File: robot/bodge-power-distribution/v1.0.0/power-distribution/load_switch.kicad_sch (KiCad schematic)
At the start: 15 parts, among them Q1 SQJA80EP-T1_GE3, Q2 SQJA80EP-T1_GE3, U1 LTC4367

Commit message: Update load switch
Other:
- note added: "Alt FETs: SQJA90EP-T1_GE3 SQJA92EP-T1_GE3"
- note added: "The voltage divider draws ~3uA, which is less than the 5uA-20uA of the LTC4367"
- note removed: "Alt: SQJA90EP-T1_GE3, SQJA92EP-T1_GE3"
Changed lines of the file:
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@@
+    (effects (font (size 1.27 1.27)) (justify left bottom))
+  )
+  (text "The voltage divider draws ~3uA,\nwhich is less than the 5uA-20uA of the LTC4367 "
+    (at 85.09 97.79 0)
     (effects (font (size 1.27 1.27)) (justify left bottom))
   )
@@
     (effects (font (size 1.27 1.27)) (justify left bottom))
   )
-  (text "Alt: SQJA90EP-T1_GE3, SQJA92EP-T1_GE3 " (at 149.86 38.1 0)
+  (text "Alt FETs:\n  SQJA90EP-T1_GE3\n  SQJA92EP-T1_GE3 " (at 147.32 36.83 0)
     (effects (font (size 1.27 1.27)) (justify left bottom))
   )

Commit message: Reorganize
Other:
- title: Power Distribution -> Bodge Control
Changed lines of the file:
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@@
   (paper "A4")
   (title_block
-    (title "Power Distribution")
-    (date "2021-11-14")
+    (title "Bodge Control")
+    (date "2022-11-06")
     (rev "1.0.0")
     (company "The A-Team (RC SSL)")

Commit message: Sync
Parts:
- added R?: 100k, Resistor_SMD:R_0402_1005Metric_Pad0.72x0.64mm_HandSolder, symbol Device:R_Small_US
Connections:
- net V_{BATT(PROTECTED)}: now also R?.1
- net ~{FAULT} renamed PGOOD_{LoadSwitch}
- net PGOOD_{LoadSwitch}: now also R?.2
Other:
- moved on the sheet: C1, C2, C3, C4, R10

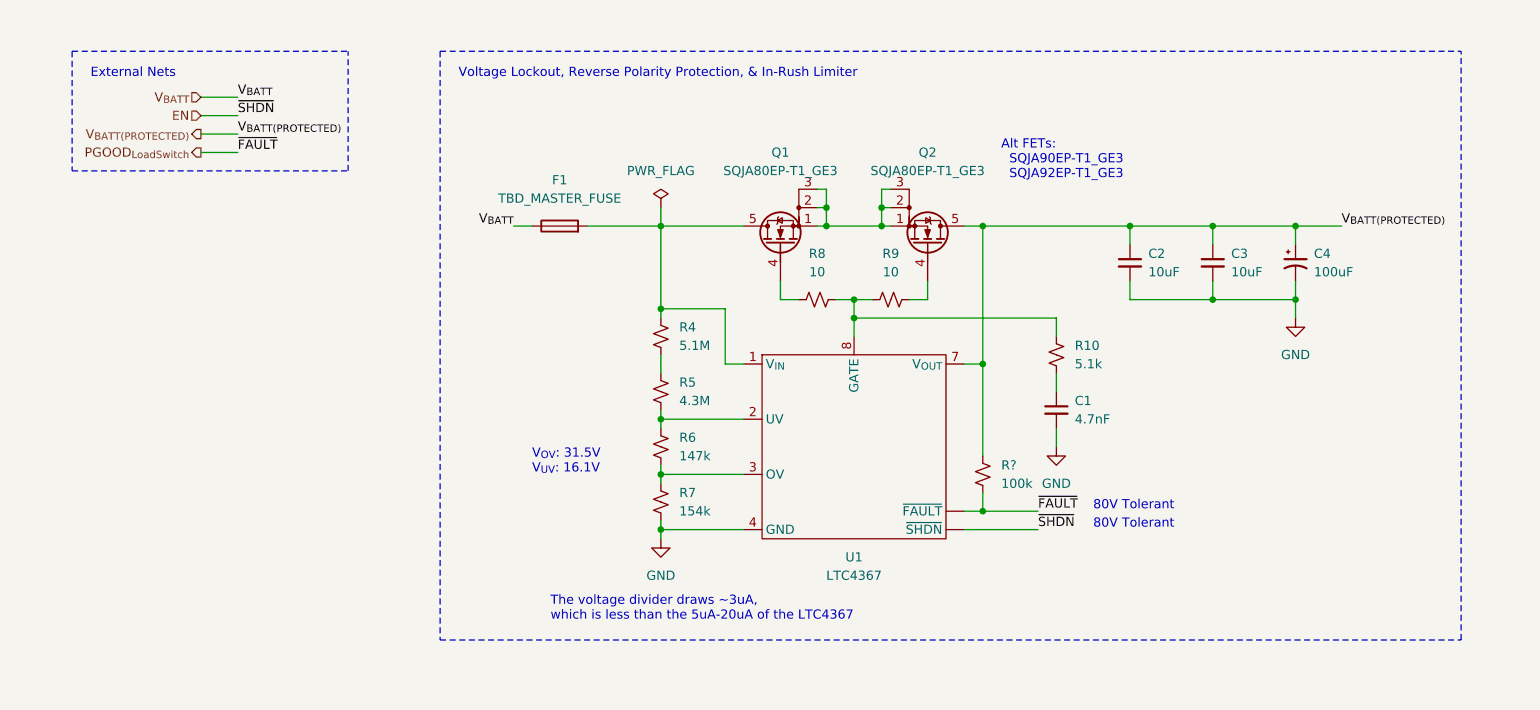
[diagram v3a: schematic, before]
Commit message: Update schematics; initial PoC layout & routing
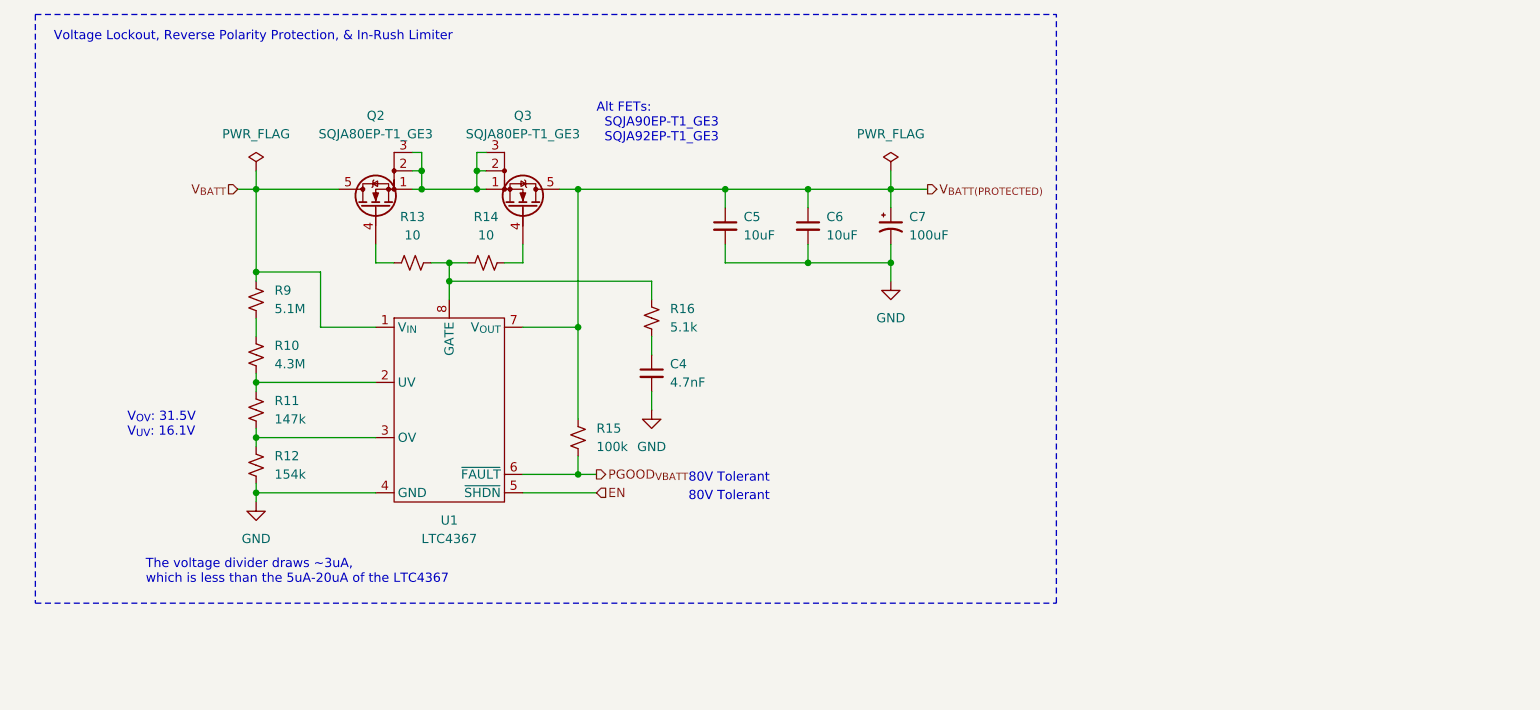
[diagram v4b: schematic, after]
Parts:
- removed F1: TBD_MASTER_FUSE, symbol Device:Fuse
- removed U1: LTC4367, symbol ltc_regulators:LTC4367
- added U1: LTC4367, AT-IC:MS8, symbol AT-PowerIC:LTC4367
- Q2: renamed from Q1; footprint Package_SO:PowerPAK_SO-8_Single -> AT-Discrete:PowerPAK_SO-8L_Single
- Q3: renamed from Q2; footprint Package_SO:PowerPAK_SO-8_Single -> AT-Discrete:PowerPAK_SO-8L_Single
- gave numbers to parts that had none: 1
- renumbered C1 to C4, C2 to C5, C3 to C6, C4 to C7, R5 to R10, R6 to R11, R7 to R12, R8 to R13, R9 to R14, R10 to R16, R4 to R9
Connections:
- net EN: now also U1.5 (~{SHDN})
- net GND: now also U1.4 (GND)
- net V_{BATT(PROTECTED)}: now also U1.7 (V_{OUT})
- net V_{BATT}: now also Q2.5 (D), R9.1, U1.1 (V_{IN})
- net at R10.2, R11.1: now also U1.2 (UV)
- net at R13.2, R14.1, R16.1: now also U1.8 (GATE)
- net at R11.2, R12.2: now also U1.3 (OV)
- net PGOOD_{LoadSwitch} renamed PGOOD_{VBATT}
- net PGOOD_{VBATT}: now also U1.6 (~{FAULT})
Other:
- note removed: "External Nets"
- moved on the sheet: C4, C5, C6, C7, Q2, Q3, R10, R11, R12, R13, R14, R15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

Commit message: Sync
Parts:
- added TP1: Inject_{+}, TestPoint:TestPoint_THTPad_2.0x2.0mm_Drill1.0mm, symbol Connector:TestPoint
- added TP2: Sense_{+}, TestPoint:TestPoint_THTPad_2.0x2.0mm_Drill1.0mm, symbol Connector:TestPoint
- added TP3: Sense_{-}, TestPoint:TestPoint_THTPad_2.0x2.0mm_Drill1.0mm, symbol Connector:TestPoint
- added TP4: Inject_{-}, TestPoint:TestPoint_THTPad_2.0x2.0mm_Drill1.0mm, symbol Connector:TestPoint
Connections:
- net V_{BATT(PROTECTED)}: now also TP1.1, TP2.1, TP3.1, TP4.1
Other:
- moved on the sheet: C5, C6, C7

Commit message: Alpha (0.0.0)
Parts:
- removed C6: 10uF, Capacitor_SMD:C_1210_3225Metric_Pad1.33x2.70mm_HandSolder, symbol Device:C_Small
- removed C7: 100uF, Capacitor_THT:CP_Radial_D10.0mm_P5.00mm, symbol Device:C_Polarized_Small_US
- removed TP1: Inject_{+}, TestPoint:TestPoint_THTPad_2.0x2.0mm_Drill1.0mm, symbol Connector:TestPoint
- removed TP2: Sense_{+}, TestPoint:TestPoint_THTPad_2.0x2.0mm_Drill1.0mm, symbol Connector:TestPoint
- removed TP3: Sense_{-}, TestPoint:TestPoint_THTPad_2.0x2.0mm_Drill1.0mm, symbol Connector:TestPoint
- removed TP4: Inject_{-}, TestPoint:TestPoint_THTPad_2.0x2.0mm_Drill1.0mm, symbol Connector:TestPoint
- C4: value 4.7nF -> 4.7nF 63V; footprint Capacitor_SMD:C_0402_1005Metric_Pad0.74x0.62mm_HandSolder -> Capacitor_SMD:C_0603_1608Metric
- C5: value 10uF -> 10uF 63V; footprint Capacitor_SMD:C_1210_3225Metric_Pad1.33x2.70mm_HandSolder -> Capacitor_SMD:C_1210_3225Metric
- renumbered R9 to R10, R10 to R11, R11 to R12, R12 to R13, R13 to R14, R14 to R15, R15 to R16, R16 to R17
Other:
- moved on the sheet: C5
